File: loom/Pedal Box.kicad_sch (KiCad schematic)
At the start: 9 parts, among them J2 APPS I/F, J51 BPS, J52 BOTS, J53 Power and Shutdown, J54 Sensors

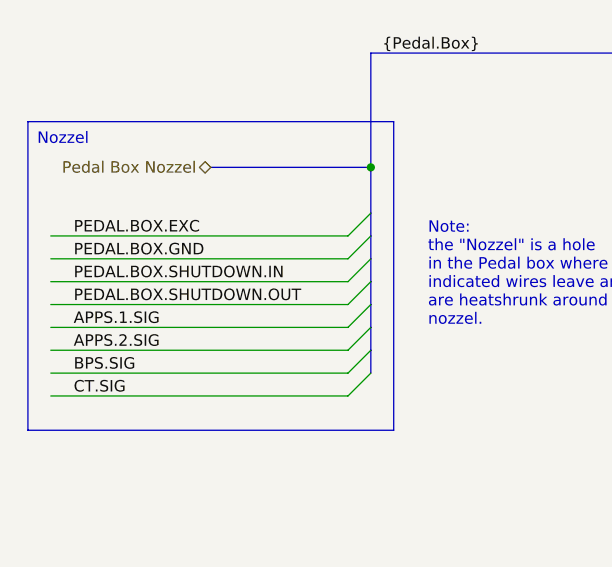
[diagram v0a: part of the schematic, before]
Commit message: fix(Loom): changed names of netlists
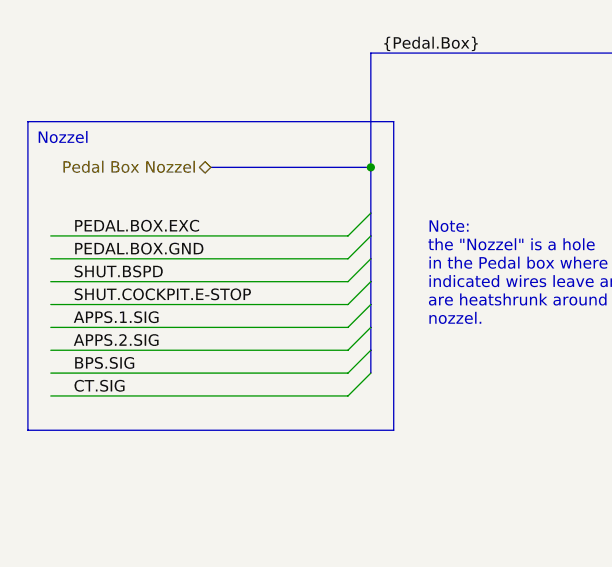
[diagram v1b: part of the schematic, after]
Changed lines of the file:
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@@
+    (effects (font (size 1.27 1.27)) (justify left bottom))
+  )
+  (label "SHUT.COCKPIT.E-STOP" (at 43.18 68.58 0) (fields_autoplaced)
     (effects (font (size 1.27 1.27)) (justify left bottom))
   )
@@
     (effects (font (size 1.27 1.27)) (justify left bottom))
   )
-  (label "PEDAL.BOX.SHUTDOWN.IN" (at 43.18 66.04 0) (fields_autoplaced)
+  (label "SHUT.BSPD" (at 43.18 66.04 0) (fields_autoplaced)
     (effects (font (size 1.27 1.27)) (justify left bottom))
   )
@@
     (effects (font (size 1.27 1.27)) (justify left bottom))
   )
-  (label "PEDAL.BOX.SHUTDOWN.OUT" (at 43.18 68.58 0) (fields_autoplaced)
-    (effects (font (size 1.27 1.27)) (justify left bottom))
-  )

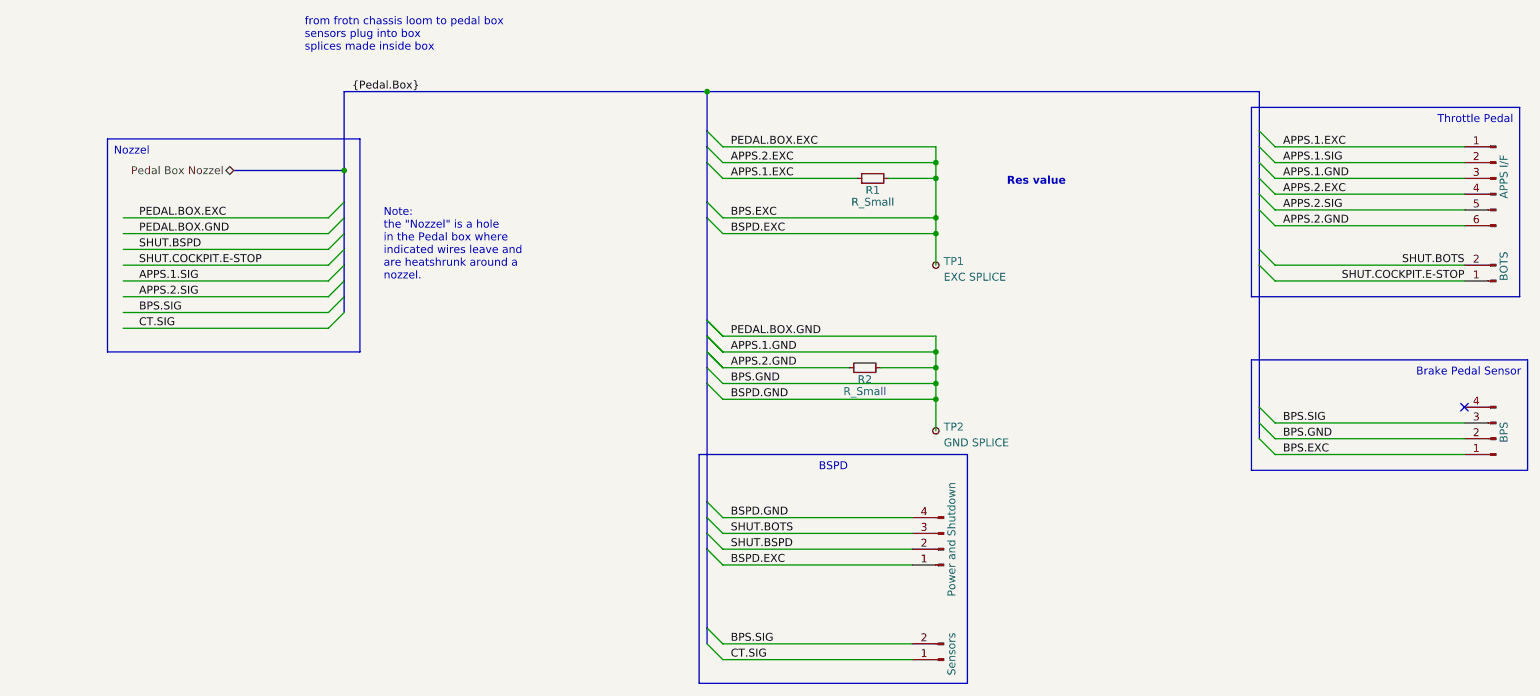
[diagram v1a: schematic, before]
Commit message: feat(Loom): Updated version of Loom Schematic
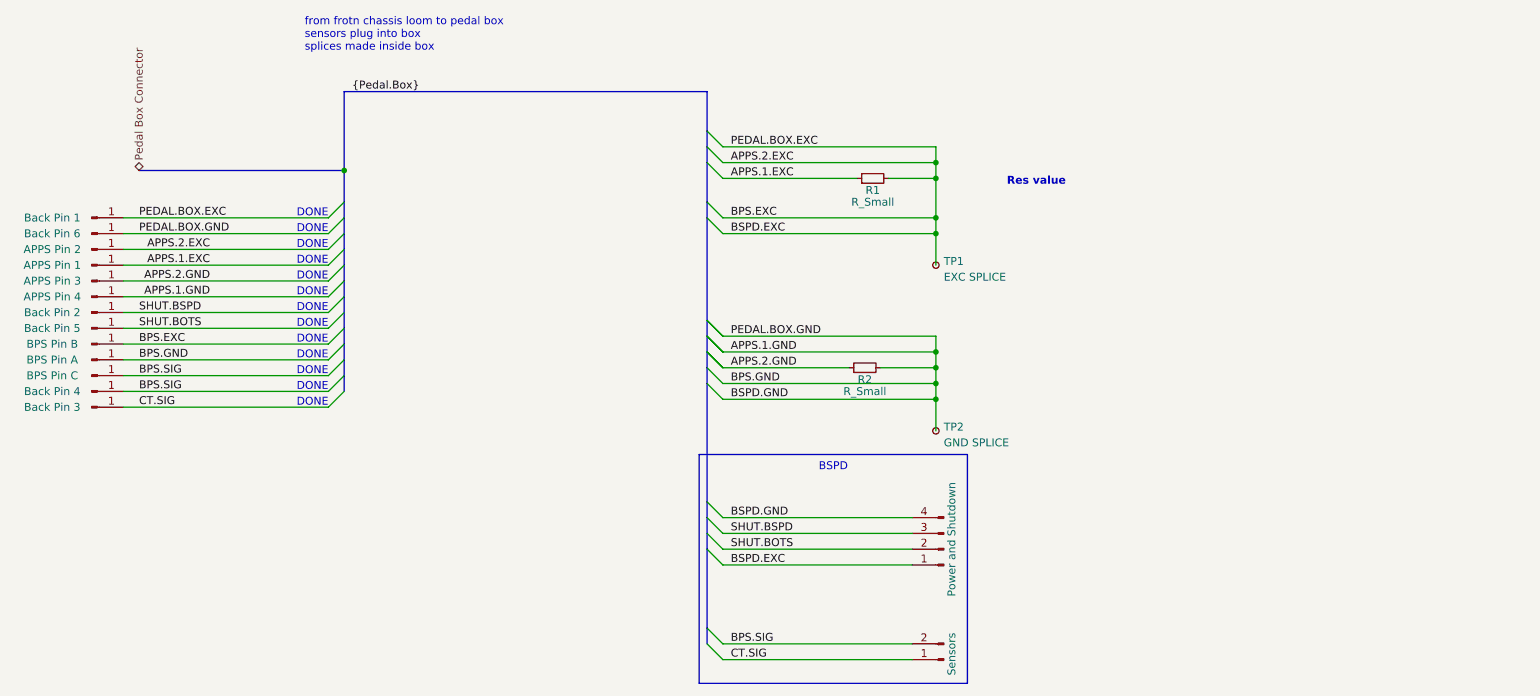
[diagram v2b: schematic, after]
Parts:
- removed J2: APPS I/F, symbol Connector:Conn_01x06_Male
- removed J51: BPS, symbol Connector:Conn_01x04_Pin
- removed J52: BOTS, symbol Connector:Conn_01x02_Pin
- added J90: BPS Pin A, symbol Connector:Conn_01x01_Pin
- added J90: APPS Pin 2, symbol Connector:Conn_01x01_Pin
- added J90: Back Pin 4, symbol Connector:Conn_01x01_Pin
- added J90: Back Pin 3, symbol Connector:Conn_01x01_Pin
- added J90: Back Pin 5, symbol Connector:Conn_01x01_Pin
- added J90: APPS Pin 3, symbol Connector:Conn_01x01_Pin
- added J90: Back Pin 1, symbol Connector:Conn_01x01_Pin
- added J90: APPS Pin 1, symbol Connector:Conn_01x01_Pin
- added J90: BPS Pin B, symbol Connector:Conn_01x01_Pin
- added J90: BPS Pin C, symbol Connector:Conn_01x01_Pin
- added J90: APPS Pin 4, symbol Connector:Conn_01x01_Pin
- added J90: Back Pin 6, symbol Connector:Conn_01x01_Pin
- added J90: Back Pin 2, symbol Connector:Conn_01x01_Pin
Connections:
- net APPS.1.EXC: now also J90.1 (Pin_1)
- net APPS.1.GND: now also J90.1 (Pin_1), J90.1 (Pin_1), J90.1 (Pin_1)
- net APPS.2.EXC: now also J90.1 (Pin_1), J90.1 (Pin_1), J90.1 (Pin_1)
- net APPS.2.GND: now also J90.1 (Pin_1)
- net BPS.SIG: now also J90.1 (Pin_1), J90.1 (Pin_1)
- net CT.SIG: now also J90.1 (Pin_1)
- net SHUT.BOTS: now also J53.2 (Pin_2), J90.1 (Pin_1); no longer J53.3 (Pin_3)
- net SHUT.BSPD: now also J53.3 (Pin_3), J90.1 (Pin_1); no longer J53.2 (Pin_2)
- no-connect marks 1 -> 0
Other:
- note added: "DONE"
- note removed: "Note: the "Nozzel" is a hole in the Pedal box where indicated wires leave and are heatshrunk around a nozzel."
